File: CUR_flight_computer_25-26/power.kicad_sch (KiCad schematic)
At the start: 28 parts, among them J2 Screw_Terminal_01x02, J3 Screw_Terminal_01x02, J4 XT30PW-M, J5 XT30PW-M, U6 BU33SD5, U7 LM66200, U8 ZXCT180A4W5, U9 ZXCT180A4W5

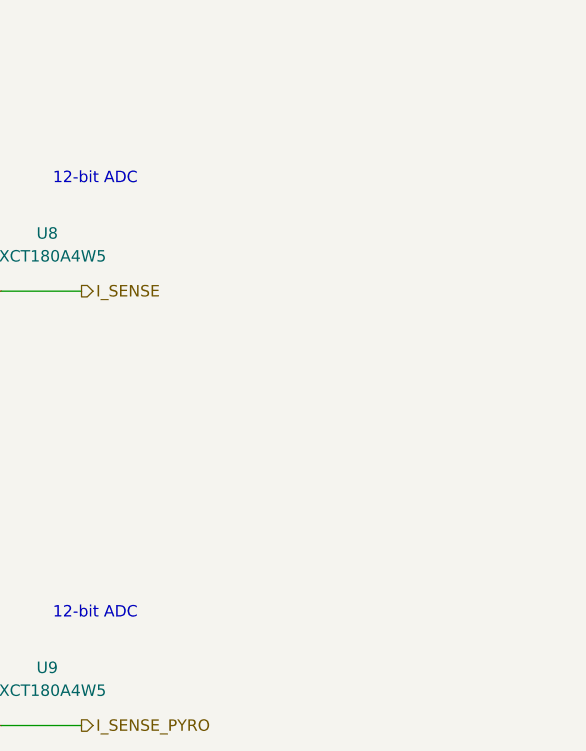
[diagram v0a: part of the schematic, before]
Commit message: added testpoints to schematic
need to update layout
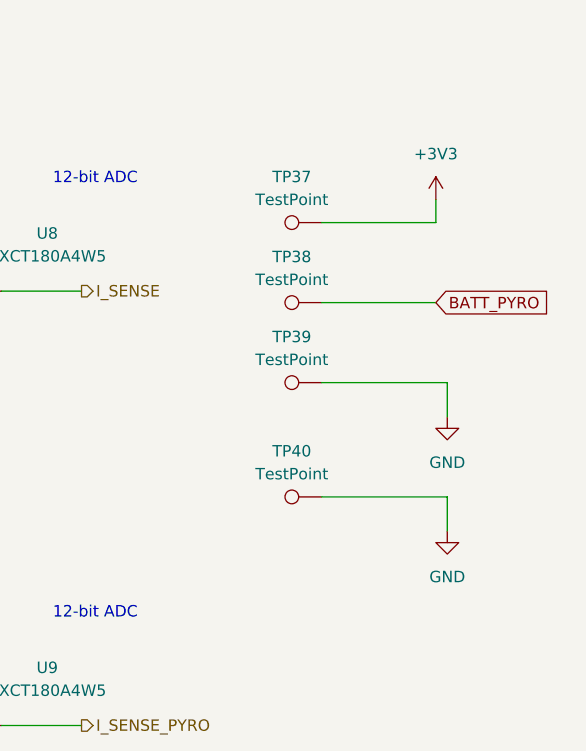
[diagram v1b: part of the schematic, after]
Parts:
- added TP37, TP38, TP39, TP40: TestPoint, TestPoint_KOASpeer:TestPoint_Chip_RCUCTE_0603, symbol Connector:TestPoint
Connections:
- net +3V3: now also TP37.1
- net BATT_PYRO: now also TP38.1
- net GND: now also TP39.1, TP40.1

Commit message: more layout yay
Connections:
- net BATT_SWITCH: now also J4.1 (Pin_1); no longer J4.2 (Pin_2)
- net GND: now also J4.2 (Pin_2), J5.2 (Pin_2); no longer J4.1 (Pin_1), J5.1 (Pin_1)
- net PYRO_BATT_SWITCH: now also J5.1 (Pin_1); no longer J5.2 (Pin_2)
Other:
- moved on the sheet: J4, J5
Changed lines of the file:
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@@
 	(symbol
 		(lib_id "Connector:Conn_01x02_Pin")
-		(at 74.93 31.75 270)
+		(at 72.39 31.75 90)
+		(mirror x)
 		(unit 1)
 		(exclude_from_sim no)
@@
 		(dnp no)
 		(property "Reference" "J5"
-			(at 71.12 31.1149 90)
+			(at 76.2 31.1149 90)
 			(effects
 				(font
@@
 		)
 		(property "Value" "XT30PW-M"
-			(at 79.248 28.194 90)
+			(at 68.072 28.194 90)
 			(effects
 				(font
@@
 		)
 		(property "Footprint" "Connector_AMASS:AMASS_XT30U-M_1x02_P5.0mm_Vertical"
-			(at 74.93 31.75 0)
+			(at 72.39 31.75 0)
 			(effects
 				(font
@@
 		)
 		(property "Datasheet" "~"
-			(at 74.93 31.75 0)
+			(at 72.39 31.75 0)
 			(effects
 				(font
@@
 		)
 		(property "Description" "Generic connector, single row, 01x02, script generated"
-			(at 74.93 31.75 0)
+			(at 72.39 31.75 0)
 			(effects
 				(font
@@
 	(symbol
 		(lib_id "Connector:Conn_01x02_Pin")
-		(at 41.91 31.75 270)
+		(at 39.37 31.75 90)
+		(mirror x)
 		(unit 1)
 		(exclude_from_sim no)
@@
 		(dnp no)
 		(property "Reference" "J4"
-			(at 38.1 31.1149 90)
+			(at 43.18 31.1149 90)
 			(effects
 				(font
@@
 		)
 		(property "Value" "XT30PW-M"
-			(at 46.228 28.194 90)
+			(at 35.052 28.194 90)
 			(effects
 				(font
@@
 		)
 		(property "Footprint" "Connector_AMASS:AMASS_XT30U-M_1x02_P5.0mm_Vertical"
-			(at 41.91 31.75 0)
+			(at 39.37 31.75 0)
 			(effects
 				(font
@@
 		)
 		(property "Datasheet" "~"
-			(at 41.91 31.75 0)
+			(at 39.37 31.75 0)
 			(effects
 				(font
@@
 		)
 		(property "Description" "Generic connector, single row, 01x02, script generated"
-			(at 41.91 31.75 0)
-			(effects
-				(font
+			(at 39.37 31.75 0)
+			(effects
+				(font

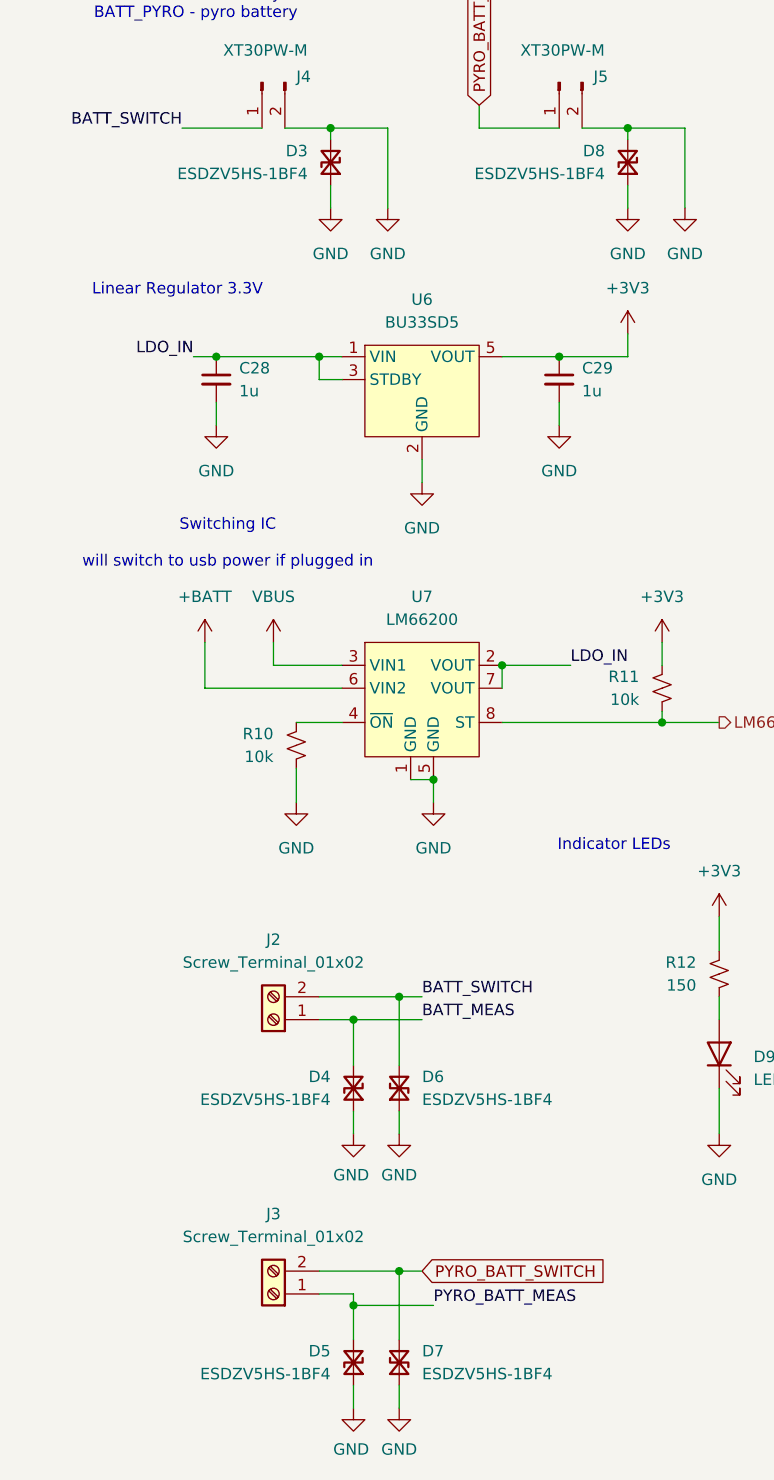
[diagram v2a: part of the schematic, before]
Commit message: updates to tvs diodes
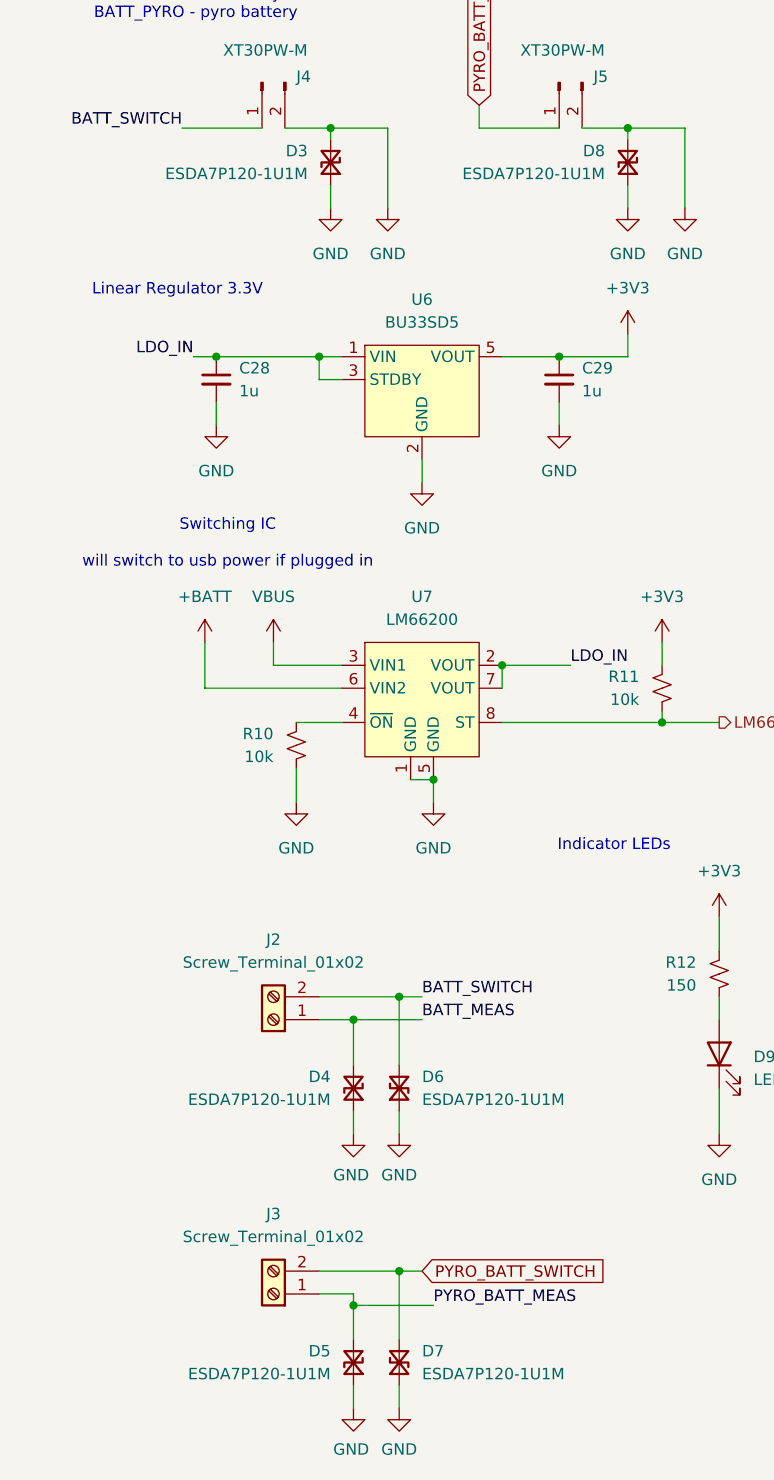
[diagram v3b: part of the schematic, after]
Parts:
- D3, D4, D5, D6, D7, D8: value ESDZV5HS-1BF4 -> ESDA7P120-1U1M
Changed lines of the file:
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@@
 			)
 		)
-		(property "Value" "ESDZV5HS-1BF4"
+		(property "Value" "ESDA7P120-1U1M"
 			(at 57.15 175.2599 90)
 			(effects
@@
 			)
 		)
-		(property "Value" "ESDZV5HS-1BF4"
+		(property "Value" "ESDA7P120-1U1M"
 			(at 46.99 175.2599 90)
 			(effects
@@
 			)
 		)
-		(property "Value" "ESDZV5HS-1BF4"
+		(property "Value" "ESDA7P120-1U1M"
 			(at 57.15 144.7799 90)
 			(effects
@@
 			)
 		)
-		(property "Value" "ESDZV5HS-1BF4"
+		(property "Value" "ESDA7P120-1U1M"
 			(at 46.99 144.7799 90)
 			(effects
@@
 			)
 		)
-		(property "Value" "ESDZV5HS-1BF4"
+		(property "Value" "ESDA7P120-1U1M"
 			(at 77.47 41.9099 90)
 			(effects
@@
 			)
 		)
-		(property "Value" "ESDZV5HS-1BF4"
+		(property "Value" "ESDA7P120-1U1M"
 			(at 44.45 41.9099 90)
 			(effects

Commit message: started traces...yay
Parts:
- D3, D4, D5, D6, D7, D8: footprint Diode_SMD:D_0201_0603Metric -> ESDA7P120:TVS_ESDA7P120-1U1M
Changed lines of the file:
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@@
 			)
 		)
-		(property "Footprint" "Diode_SMD:D_0201_0603Metric"
+		(property "Footprint" "ESDA7P120:TVS_ESDA7P120-1U1M"
 			(at 54.61 173.99 0)
 			(effects
@@
 			)
 		)
-		(property "Footprint" "Diode_SMD:D_0201_0603Metric"
+		(property "Footprint" "ESDA7P120:TVS_ESDA7P120-1U1M"
 			(at 49.53 173.99 0)
 			(effects
@@
 			)
 		)
-		(property "Footprint" "Diode_SMD:D_0201_0603Metric"
+		(property "Footprint" "ESDA7P120:TVS_ESDA7P120-1U1M"
 			(at 54.61 143.51 0)
 			(effects
@@
 			)
 		)
-		(property "Footprint" "Diode_SMD:D_0201_0603Metric"
+		(property "Footprint" "ESDA7P120:TVS_ESDA7P120-1U1M"
 			(at 49.53 143.51 0)
 			(effects
@@
 			)
 		)
-		(property "Footprint" "Diode_SMD:D_0201_0603Metric"
+		(property "Footprint" "ESDA7P120:TVS_ESDA7P120-1U1M"
 			(at 80.01 40.64 0)
 			(effects
@@
 			)
 		)
-		(property "Footprint" "Diode_SMD:D_0201_0603Metric"
+		(property "Footprint" "ESDA7P120:TVS_ESDA7P120-1U1M"
 			(at 46.99 40.64 0)
 			(effects

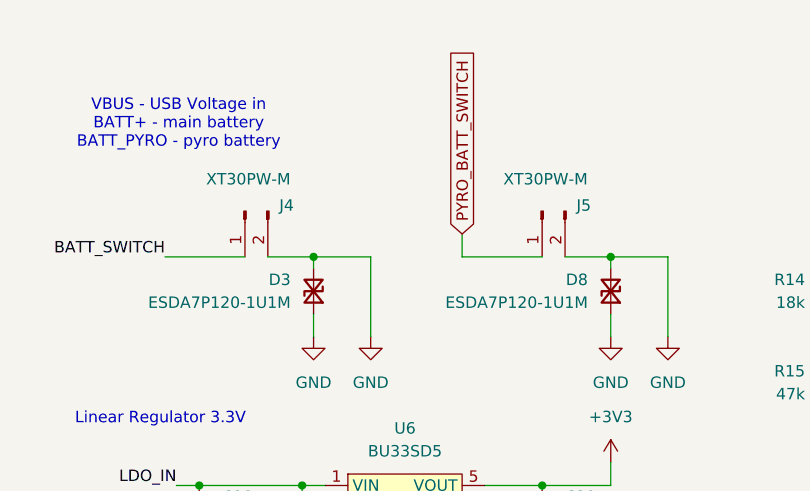
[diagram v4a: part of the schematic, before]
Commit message: started routing power and rf section
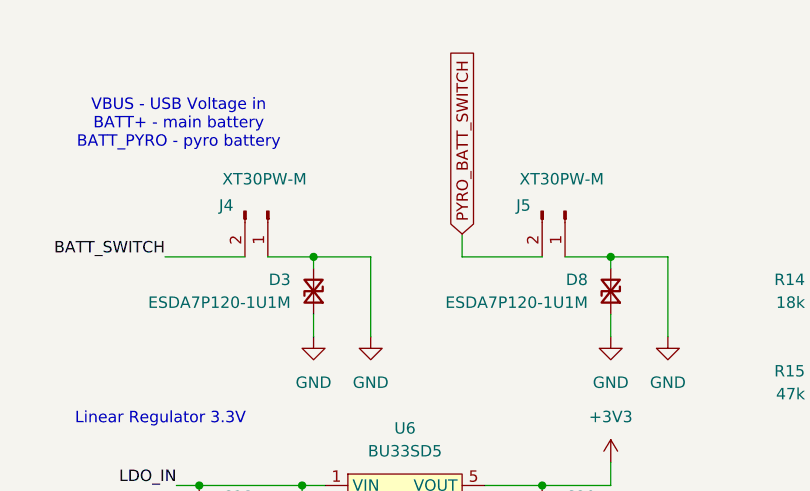
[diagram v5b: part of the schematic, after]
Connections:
- net BATT_SWITCH: now also J4.2 (Pin_2); no longer J4.1 (Pin_1)
- net GND: now also J4.1 (Pin_1), J5.1 (Pin_1); no longer J4.2 (Pin_2), J5.2 (Pin_2)
- net PYRO_BATT_SWITCH: now also J5.2 (Pin_2); no longer J5.1 (Pin_1)
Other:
- moved on the sheet: J4, J5
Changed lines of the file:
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@@
 		)
 	)
-	(label "PYRO_BATT_MEAS"
-		(at 133.35 33.02 90)
+	(label "BATT_MEAS"
+		(at 57.15 135.89 0)
 		(effects
 			(font
@@
 		)
 	)
-	(label "BATT_MEAS"
-		(at 185.42 34.29 90)
+	(label "PYRO_BATT_MEAS"
+		(at 133.35 33.02 90)
 		(effects
 			(font
@@
 		)
 	)
-	(label "BATT_SWITCH"
-		(at 57.15 133.35 0)
+	(label "BATT_MEAS"
+		(at 185.42 34.29 90)
 		(effects
 			(font
@@
 		)
 	)
-	(label "BATT_MEAS"
-		(at 57.15 135.89 0)
+	(label "BATT_SWITCH"
+		(at 57.15 133.35 0)
 		(effects
 			(font
@@
 	(symbol
 		(lib_id "Connector:Conn_01x02_Pin")
-		(at 72.39 31.75 90)
-		(mirror x)
+		(at 74.93 31.75 270)
 		(unit 1)
 		(exclude_from_sim no)
@@
 		(dnp no)
 		(property "Reference" "J5"
-			(at 76.2 31.1149 90)
+			(at 71.12 31.1149 90)
 			(effects
 				(font
@@
 		)
 		(property "Value" "XT30PW-M"
-			(at 68.072 28.194 90)
+			(at 79.248 28.194 90)
 			(effects
 				(font
@@
 		)
 		(property "Footprint" "Connector_AMASS:AMASS_XT30U-M_1x02_P5.0mm_Vertical"
-			(at 72.39 31.75 0)
+			(at 74.93 31.75 0)
 			(effects
 				(font
@@
 		)
 		(property "Datasheet" "~"
-			(at 72.39 31.75 0)
+			(at 74.93 31.75 0)
 			(effects
 				(font
@@
 		)
 		(property "Description" "Generic connector, single row, 01x02, script generated"
-			(at 72.39 31.75 0)
+			(at 74.93 31.75 0)
 			(effects
 				(font
@@
 	(symbol
 		(lib_id "Connector:Conn_01x02_Pin")
-		(at 39.37 31.75 90)
-		(mirror x)
+		(at 41.91 31.75 270)
 		(unit 1)
 		(exclude_from_sim no)
@@
 		(dnp no)
 		(property "Reference" "J4"
-			(at 43.18 31.1149 90)
+			(at 38.1 31.1149 90)
 			(effects
 				(font
@@
 		)
 		(property "Value" "XT30PW-M"
-			(at 35.052 28.194 90)
+			(at 46.228 28.194 90)
 			(effects
 				(font
@@
 		)
 		(property "Footprint" "Connector_AMASS:AMASS_XT30U-M_1x02_P5.0mm_Vertical"
-			(at 39.37 31.75 0)
+			(at 41.91 31.75 0)
 			(effects
 				(font
@@
 		)
 		(property "Datasheet" "~"
-			(at 39.37 31.75 0)
+			(at 41.91 31.75 0)
 			(effects
 				(font
@@
 		)
 		(property "Description" "Generic connector, single row, 01x02, script generated"
-			(at 39.37 31.75 0)
+			(at 41.91 31.75 0)
 			(effects
 				(font

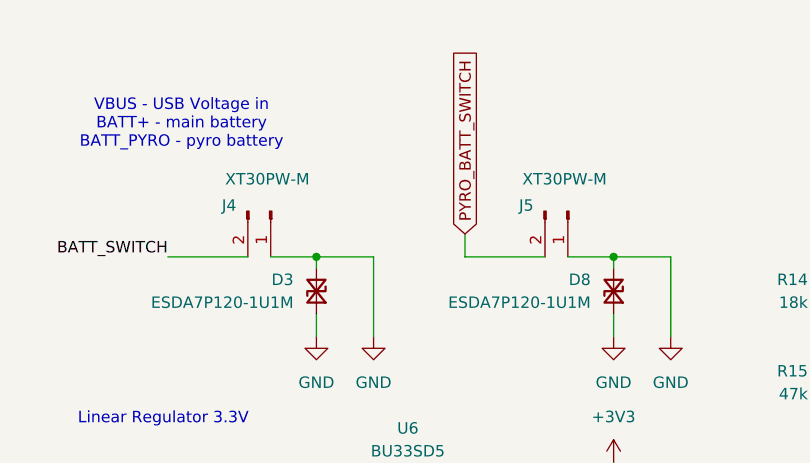
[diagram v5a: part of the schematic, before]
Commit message: restart layout, downsize mounting holes
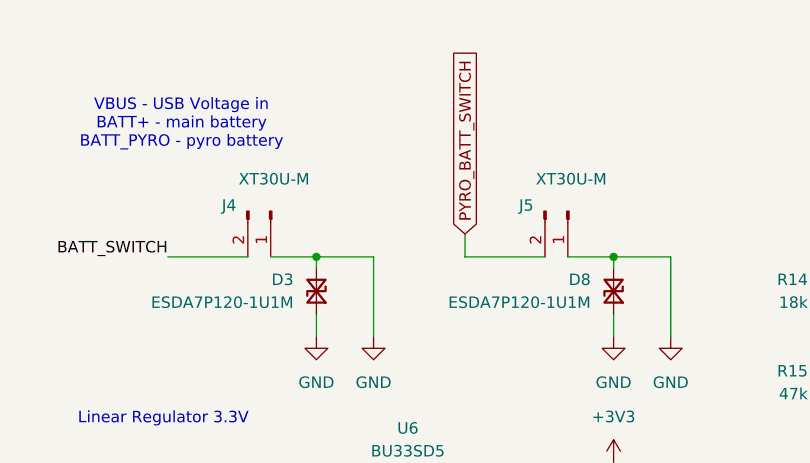
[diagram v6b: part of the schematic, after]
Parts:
- J4, J5: value XT30PW-M -> XT30U-M
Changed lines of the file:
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@@
 			)
 		)
-		(property "Value" "XT30PW-M"
+		(property "Value" "XT30U-M"
 			(at 79.248 28.194 90)
 			(effects
@@
 			)
 		)
-		(property "Value" "XT30PW-M"
+		(property "Value" "XT30U-M"
 			(at 46.228 28.194 90)
 			(effects

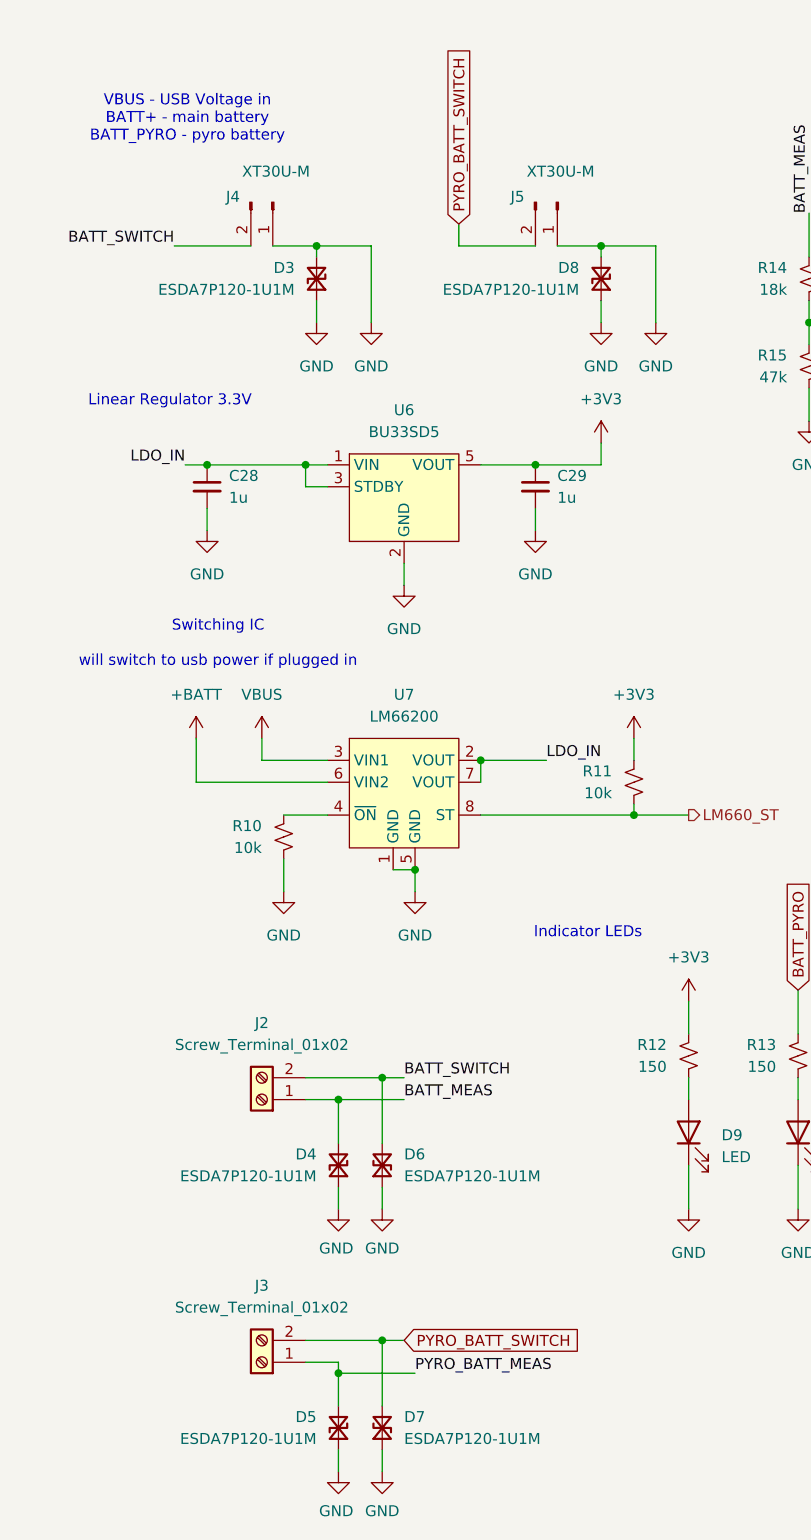
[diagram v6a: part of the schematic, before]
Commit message: Remove ESD protection on power
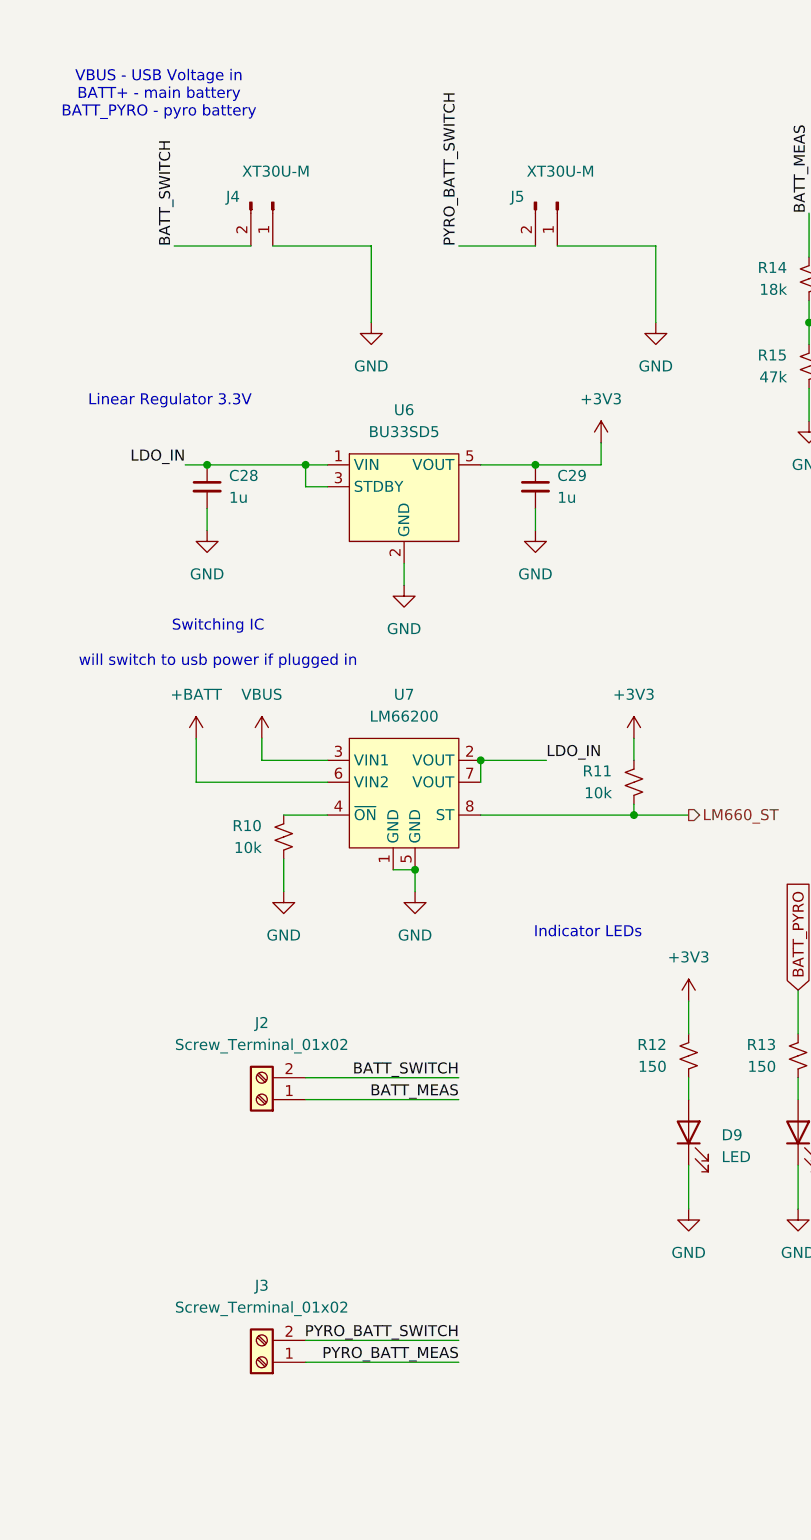
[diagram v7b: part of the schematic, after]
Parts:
- removed D3, D4, D5, D6, D7, D8: ESDA7P120-1U1M, ESDA7P120:TVS_ESDA7P120-1U1M, symbol Device:D_TVS_Small
